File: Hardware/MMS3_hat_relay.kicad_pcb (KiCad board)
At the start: 2 copper layers, 100 x 50 mm, 85 parts, among them CN1 DB2ERC-5.0-3P-GN, CN2 DB2ERC-5.0-3P-GN, CN3 DB2ERC-5.0-3P-GN, CN4 DB2ERC-5.0-3P-GN, CN5 DB2ERC-5.0-3P-GN, J1 Chainbus in, J2 Chainbus Out, J3 Conn_01x04_Pin, J5 Program, Q12 MMBT5551 200-300, Q13 MMBT5551 200-300, Q14 MMBT5551 200-300, Q15 MMBT5551 200-300, Q16 MMBT5551 200-300, U1 SN74CB3Q3384APW, U2 M24C64, U3 CH32V003FxPx, U4 AMS1117, U5 LTV-217-B-G, U6 LTV-217-B-G, U7 LTV-217-B-G, U8 LTV-217-B-G, U9 LTV-217-B-G, X1 X322525MOB4SI

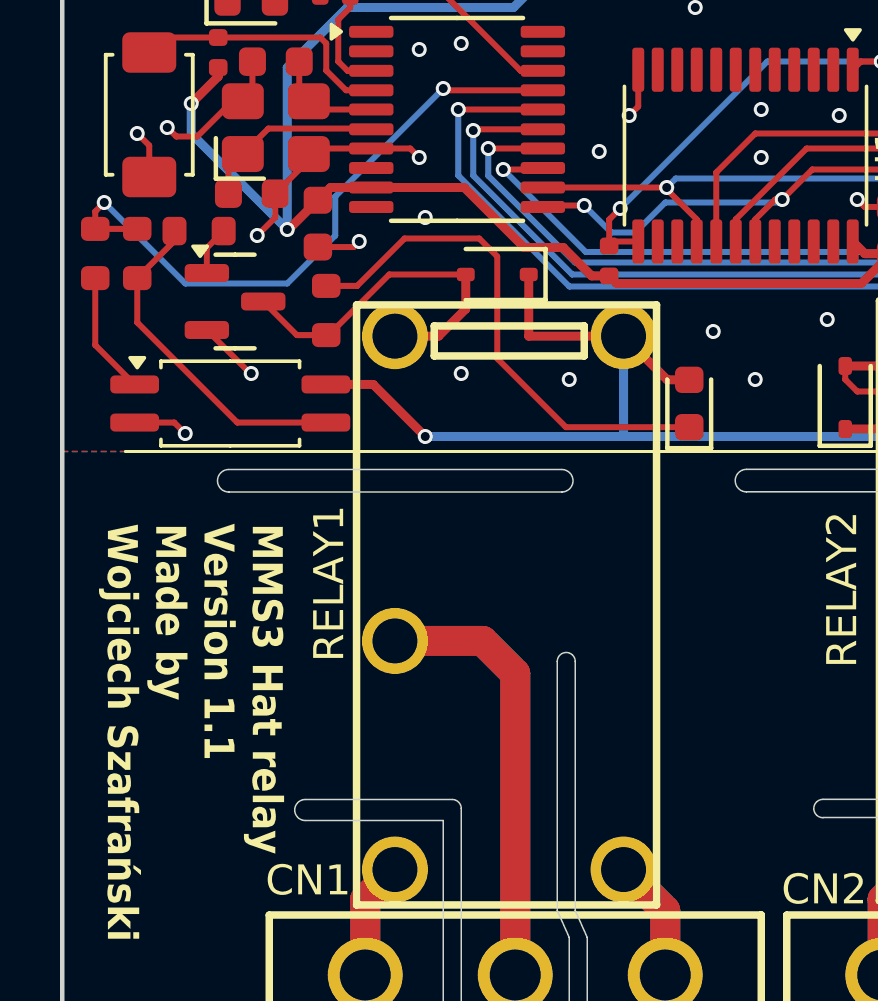
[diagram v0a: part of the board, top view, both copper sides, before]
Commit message: Ver 1.2 - Fixed SDA SCL mixup
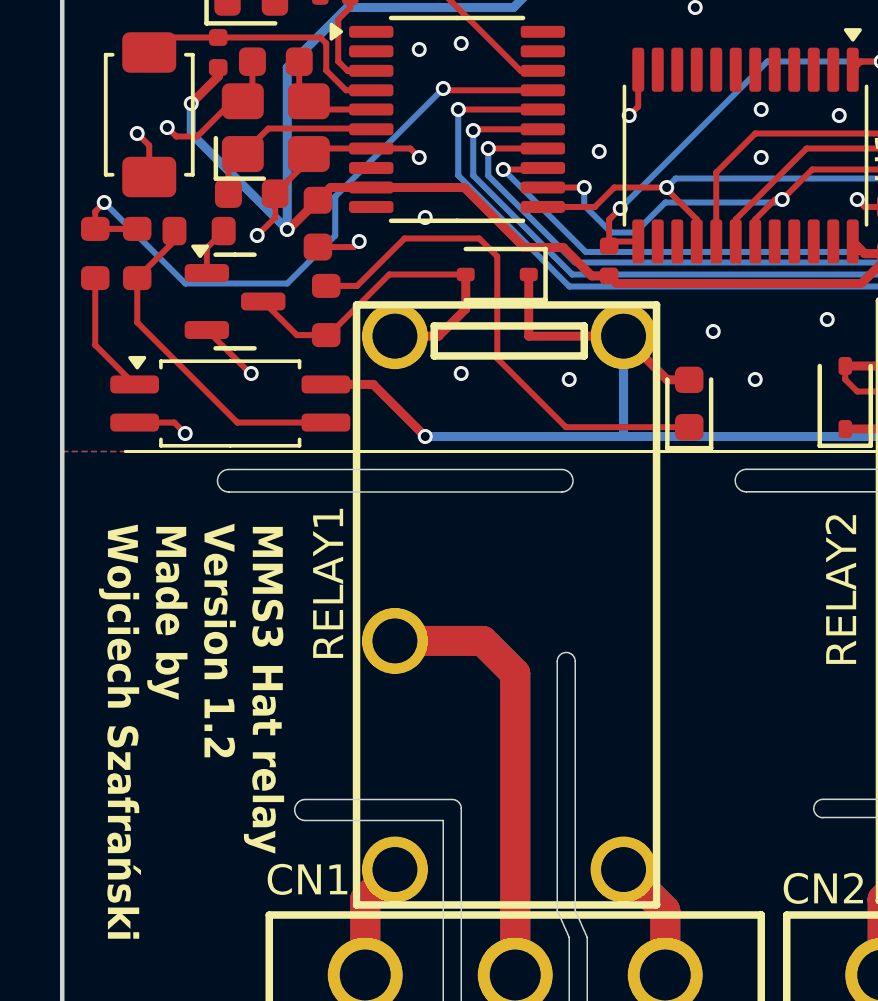
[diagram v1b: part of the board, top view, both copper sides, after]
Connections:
- U3 pad 11: /Chainbus.SCL -> /Chainbus.SDA
- U3 pad 12: /Chainbus.SDA -> /Chainbus.SCL
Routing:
- net /Chainbus.SCL: track 90.8 -> 91.4 mm
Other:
- board text added: "MMS3 Hat relay Version 1.2 Made by Wojciech Szafrański"
- board text removed: "MMS3 Hat relay Version 1.1 Made by Wojciech Szafrański"
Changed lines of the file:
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@@
 	(title_block
 		(title "MMS3 Hat Relay")
-		(date "2026-06-08")
-		(rev "1.1")
+		(date "2026-08-11")
+		(rev "1.2")
 		(comment 1 "Made by Wojciech Szafrański")
 		(comment 2 "Designed in poland")
@@
 			(layers "F.Cu" "F.Mask" "F.Paste")
 			(roundrect_rratio 0.25)
-			(net "/Chainbus.SCL")
+			(net "/Chainbus.SDA")
 			(pinfunction "PC1_11")
 			(pintype "bidirectional")
@@
 			(layers "F.Cu" "F.Mask" "F.Paste")
 			(roundrect_rratio 0.25)
-			(net "/Chainbus.SDA")
+			(net "/Chainbus.SCL")
 			(pinfunction "PC2_12")
 			(pintype "bidirectional")
@@
 		(layer "User.4")
 	)
-	(gr_text "MMS3 Hat relay\nVersion 1.1\nMade by \nWojciech Szafrański"
+	(gr_text "MMS3 Hat relay\nVersion 1.2\nMade by \nWojciech Szafrański"
 		(at 82.5 113.4 270)
 		(layer "F.SilkS")
@@
 	)
 	(segment
-		(start 95.5 102.8)
-		(end 94.17 102.8)
-		(width 0.2)
-		(layer "F.Cu")
-		(net "/Chainbus.SCL")
-	)
-	(segment
 		(start 101.2 103.262501)
 		(end 101.862501 102.6)
@@
 	)
 	(segment
-		(start 94.17 102.8)
-		(end 94.12 102.85)
+		(start 94.12 102.2)
+		(end 95.5 102.2)
 		(width 0.2)
 		(layer "F.Cu")
@@
 	)
 	(via
-		(at 102.1 102.6)
+		(at 95.5 102.2)
 		(size 0.5)
 		(drill 0.3)
@@
 	)
 	(via
-		(at 95.5 102.8)
+		(at 102.1 102.6)
 		(size 0.5)
 		(drill 0.3)
@@
 	)
 	(segment
+		(start 95.5 102.2)
+		(end 95.5 102.8)
+		(width 0.2)
+		(layer "B.Cu")
+		(net "/Chainbus.SCL")
+	)
+	(segment
 		(start 102.1 102.6)
 		(end 102 102.7)
@@
 	)
 	(segment
-		(start 98.187499 102.2)
-		(end 94.12 102.2)
-		(width 0.2)
-		(layer "F.Cu")
-		(net "/Chainbus.SDA")
-	)
-	(segment
 		(start 170.6 105)
 		(end 173.82 108.22)
@@
 	)
 	(segment
+		(start 95.85 102.85)
+		(end 94.12 102.85)
+		(width 0.2)
+		(layer "F.Cu")
+		(net "/Chainbus.SDA")
+	)
+	(segment
 		(start 98.243749 102.205308)
 		(end 98.249057 102.2)
@@
 	)
 	(segment
+		(start 96.5 102.2)
+		(end 95.85 102.85)
+		(width 0.2)
+		(layer "F.Cu")
+		(net "/Chainbus.SDA")
+	)
+	(segment
+		(start 94.17 102.8)
+		(end 94.12 102.85)
+		(width 0.2)
+		(layer "F.Cu")
+		(net "/Chainbus.SDA")
+	)
+	(segment
 		(start 173.82 108.22)
 		(end 175.895 108.22)
@@
 		(width 0.2)
 		(layer "F.Cu")
+		(net "/Chainbus.SDA")
+	)
+	(segment
+		(start 98.249057 102.2)
+		(end 96.5 102.2)
+		(width 0.2)
+		(layer "F.Cu")

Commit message: fixed res pins
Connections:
- J1 pad 25: unconnected-(J1-Pin_25-Pad25) -> /Interboard_connector/R1
- J1 pad 27: unconnected-(J1-Pin_27-Pad27) -> /Interboard_connector/R2
- J2 pad 25: unconnected-(J2-Pin_25-Pad25) -> /Interboard_connector/R1
- J2 pad 27: unconnected-(J2-Pin_27-Pad27) -> /Interboard_connector/R2
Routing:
- net /Interboard_connector/R1: track 0.00 -> 3.42 mm, vias 0 -> 1
- net /Interboard_connector/R2: track 0.00 -> 3.32 mm, vias 0 -> 1
